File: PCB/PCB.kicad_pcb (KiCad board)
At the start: 2 copper layers, 120 x 60 mm, 62 parts, among them J1 USB_C_Receptacle_USB2.0_16P, J2 Conn_01x15, J3 Conn_01x15, Q2 IRLML2060, SW1 TSA016A2526B, SW2 TSA016A2526B, SW3 TSA016A2526B, U1 RP2040, U2 USBLC6-2SC6, U3 NCP1117ST33T3G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

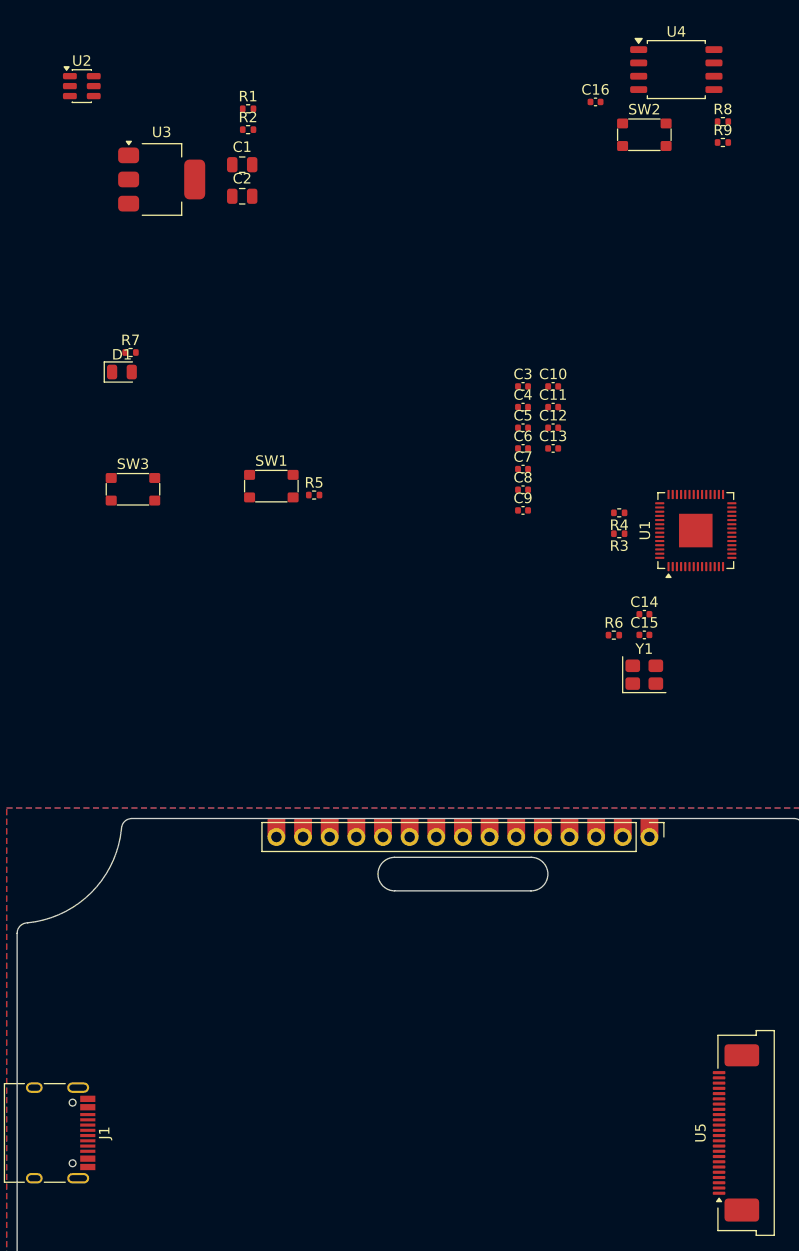
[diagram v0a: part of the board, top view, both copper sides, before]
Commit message: re-wiring a bit for easy routing
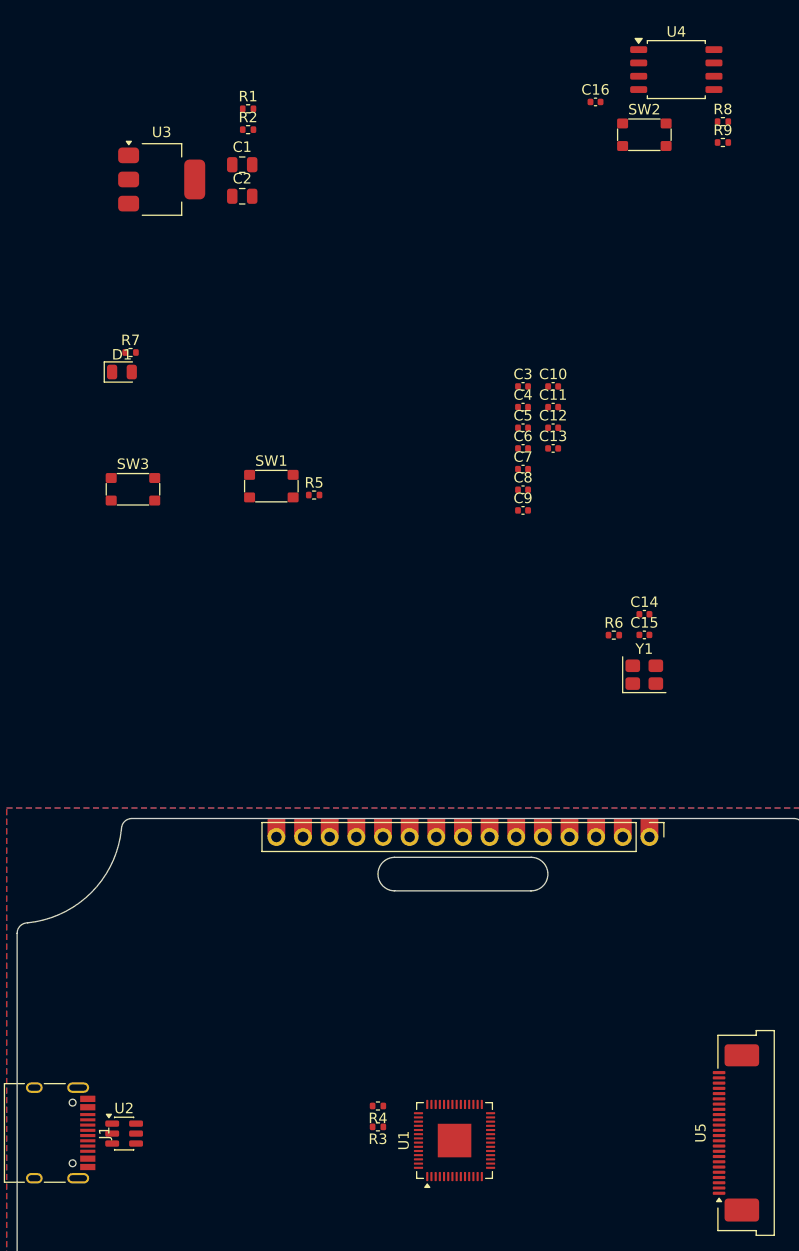
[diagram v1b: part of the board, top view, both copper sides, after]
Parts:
- moved U2 99.9 mm to (80.2, 125.0)
- moved U1 62.5 mm to (111.7, 125.7)
- moved R3 61.0 mm to (104.4, 124.4)
- moved R4 61.0 mm to (104.4, 122.4)
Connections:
- J2 pad 10: /GPIO15 -> /GPIO5
- J2 pad 11: /GPIO16 -> /GPIO6
- J2 pad 12: /GPIO17 -> /GPIO7
- J2 pad 14: /GPIO18 -> /GPIO8
- J2 pad 15: /GPIO19 -> /GPIO9
- J2 pad 2: /GPIO10 -> /GPIO0
- J2 pad 4: /GPIO11 -> /GPIO1
- J2 pad 6: /GPIO12 -> /GPIO2
- J2 pad 7: /GPIO13 -> /GPIO3
- J2 pad 9: /GPIO14 -> /GPIO4
- U1 pad 11: /NFC_GPO -> /GPIO8
- U1 pad 13: /GPIO10 -> /GPIO9
- U1 pad 14: /GPIO11 -> /NFC_SDA
- U1 pad 15: /GPIO12 -> /NFC_SCL
- U1 pad 16: /GPIO13 -> /NFC_GPO
- U1 pad 17: /GPIO14 -> /EPD_DC
- U1 pad 18: /GPIO15 -> /EPD_SCK
- U1 pad 2: /EPD_BUSY -> /GPIO0
- U1 pad 27: /GPIO16 -> /EPD_MOSI
- U1 pad 28: /GPIO17 -> /EPD_BUSY
- U1 pad 29: /GPIO18 -> /EPD_CS
- U1 pad 3: /EPD_CS -> /GPIO1
- U1 pad 30: /GPIO19 -> /EPD_RST
- U1 pad 4: /EPD_SCK -> /GPIO2
- U1 pad 5: /EPD_MOSI -> /GPIO3
- U1 pad 6: /EPD_RST -> /GPIO4
- U1 pad 7: /EPD_DC -> /GPIO5
- U1 pad 8: /NFC_SDA -> /GPIO6
- U1 pad 9: /NFC_SCL -> /GPIO7

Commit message: re-wiring some more stuff, also laying out some stuff
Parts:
- moved C16 150.3 mm to (78.1, 169.4)
- moved R8 150.3 mm to (90.2, 171.3)
- moved R9 150.3 mm to (90.2, 173.3)
- moved SW2 150.3 mm to (82.7, 172.5)
- moved U4 110.2 mm to (104.4, 130.1), turned to 90 degrees
- moved R4 1.97 mm to (106.2, 123.2)
- moved R3 1.81 mm to (106.2, 124.2)
- moved U1 0.91 mm to (111.7, 124.8)
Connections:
- U1 pad 17: /EPD_DC -> /EPD_BUSY
- U1 pad 28: /EPD_BUSY -> /EPD_DC
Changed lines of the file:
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@@
 	(footprint "Capacitor_SMD:C_0402_1005Metric"
 		(layer "F.Cu")
-		(at 125.14 26.69)
+		(at 78.09 169.39)
 		(descr "Capacitor SMD 0402 (1005 Metric), square (rectangular) end terminal, IPC-7351 nominal, (Body size source: IPC-SM-782 page 76, https://www.pcb-3d.com/wordpress/wp-content/uploads/ipc-sm-782a_amendment_1_and_2.pdf), generated with kicad-footprint-generator")
 		(tags "capacitor")
@@
 	(footprint "Package_DFN_QFN:QFN-56-1EP_7x7mm_P0.4mm_EP3.2x3.2mm"
 		(layer "F.Cu")
-		(at 111.7 125.698 90)
+		(at 111.7 124.788998 90)
 		(descr "QFN, 56 Pin (https://datasheets.raspberrypi.com/rp2040/rp2040-datasheet.pdf#page=607), generated with kicad-footprint-generator ipc_noLead_generator.py")
 		(tags "QFN NoLead")
@@
 			(layers "F.Cu" "F.Mask" "F.Paste")
 			(roundrect_rratio 0.25)
-			(net 49 "/EPD_DC")
+			(net 59 "/EPD_BUSY")
 			(pinfunction "GPIO14")
 			(pintype "bidirectional")
@@
 			(layers "F.Cu" "F.Mask" "F.Paste")
 			(roundrect_rratio 0.25)
-			(net 59 "/EPD_BUSY")
+			(net 49 "/EPD_DC")
 			(pinfunction "GPIO17")
 			(pintype "bidirectional")
@@
 	(footprint "Package_SO:SOIC-8_5.3x5.3mm_P1.27mm"
 		(layer "F.Cu")
-		(at 132.8425 23.605)
+		(at 104.4 130.05 90)
 		(descr "SOIC, 8 Pin (JEITA/EIAJ ED-7311-19 variation 08-001-BBA and Atmel/Microchip, 208 mils width, https://www.jeita.or.jp/japanese/standard/book/ED-7311-19/#target/page_no=21, https://ww1.microchip.com/downloads/en/DeviceDoc/20005045C.pdf#page=23, https://ww1.microchip.com/downloads/en/DeviceDoc/doc2535.pdf#page=162), generated with kicad-footprint-generator ipc_gullwing_generator.py")
 		(tags "SOIC SO P-SOP SOP SOP-8 SO SO-8 8S2 S2AE/F K04-056 CASE-751BE SO8W 8-Pin-SOIC PSA W8-2 W8-4 W8MS-1 FPT-8P-M08")
 		(property "Reference" "U4"
-			(at 0 -3.6 0)
+			(at 0 -3.6 90)
 			(layer "F.SilkS")
 			(effects
@@
 		)
 		(property "Value" "W25Q32JVSS"
-			(at 0 3.6 0)
+			(at 0 3.6 90)
 			(layer "F.Fab")
 			(effects
@@
 		)
 		(property "Datasheet" "http://www.winbond.com/resource-files/w25q32jv%20revg%2003272018%20plus.pdf"
-			(at 0 0 0)
+			(at 0 0 90)
 			(layer "F.Fab")
 			(hide yes)
@@
 		)
 		(property "Description" "32Mbit / 4MiB Serial Flash Memory, Standard/Dual/Quad SPI, 2.7-3.6V, SOIC-8 (208 mil)"
-			(at 0 0 0)
+			(at 0 0 90)
 			(layer "F.Fab")
 			(hide yes)
@@
 		(attr smd)
 		(fp_line
-			(start -2.76 -2.76)
-			(end 2.76 -2.76)
+			(start 2.76 -2.76)
+			(end 2.76 -2.49)
 			(stroke
 				(width 0.12)
@@
 		)
 		(fp_line
-			(start -2.76 -2.49)
-			(end -2.76 -2.76)
+			(start -2.76 -2.76)
+			(end 2.76 -2.76)
 			(stroke
 				(width 0.12)
@@
 		)
 		(fp_line
-			(start -2.76 2.76)
-			(end -2.76 2.49)
+			(start -2.76 -2.49)
+			(end -2.76 -2.76)
 			(stroke
 				(width 0.12)
@@
 		)
 		(fp_line
-			(start 2.76 -2.76)
-			(end 2.76 -2.49)
+			(start 2.76 2.49)
+			(end 2.76 2.76)
 			(stroke
 				(width 0.12)
@@
 		)
 		(fp_line
-			(start 2.76 2.49)
-			(end 2.76 2.76)
+			(start 2.76 2.76)
+			(end -2.76 2.76)
 			(stroke
 				(width 0.12)
@@
 		)
 		(fp_line
-			(start 2.76 2.76)
-			(end -2.76 2.76)
+			(start -2.76 2.76)
+			(end -2.76 2.49)
 			(stroke
 				(width 0.12)
@@
 		)
 		(fp_line
-			(start -4.65 -2.48)
-			(end -2.9 -2.48)
+			(start 2.9 -2.9)
+			(end 2.9 -2.48)
 			(stroke
 				(width 0.05)
@@
 		)
 		(fp_line
-			(start -4.65 2.48)
-			(end -4.65 -2.48)
+			(start -2.9 -2.9)
+			(end 2.9 -2.9)
 			(stroke
 				(width 0.05)
@@
 		)
 		(fp_line
-			(start -2.9 -2.9)
-			(end 2.9 -2.9)
+			(start 4.65 -2.48)
+			(end 4.65 2.48)
 			(stroke
 				(width 0.05)
@@
 		)
 		(fp_line
-			(start -2.9 -2.48)
-			(end -2.9 -2.9)
+			(start 2.9 -2.48)
+			(end 4.65 -2.48)
 			(stroke
 				(width 0.05)
@@
 		)
 		(fp_line
-			(start -2.9 2.48)
-			(end -4.65 2.48)
+			(start -2.9 -2.48)
+			(end -2.9 -2.9)
 			(stroke
 				(width 0.05)
@@
 		)
 		(fp_line
-			(start -2.9 2.9)
-			(end -2.9 2.48)
+			(start -4.65 -2.48)
+			(end -2.9 -2.48)
 			(stroke
 				(width 0.05)
@@
 		)
 		(fp_line
-			(start 2.9 -2.9)
-			(end 2.9 -2.48)
+			(start 4.65 2.48)
+			(end 2.9 2.48)
 			(stroke
 				(width 0.05)
@@
 		)
 		(fp_line
-			(start 2.9 -2.48)
-			(end 4.65 -2.48)
+			(start 2.9 2.48)
+			(end 2.9 2.9)
 			(stroke
 				(width 0.05)
@@
 		)
 		(fp_line
-			(start 2.9 2.48)
-			(end 2.9 2.9)
+			(start -2.9 2.48)
+			(end -4.65 2.48)
 			(stroke
 				(width 0.05)
@@
 		)
 		(fp_line
-			(start 2.9 2.9)
-			(end -2.9 2.9)
+			(start -4.65 2.48)
+			(end -4.65 -2.48)
 			(stroke
 				(width 0.05)
@@
 		)
 		(fp_line
-			(start 4.65 -2.48)
-			(end 4.65 2.48)
+			(start 2.9 2.9)
+			(end -2.9 2.9)
 			(stroke
 				(width 0.05)
@@
 		)
 		(fp_line
-			(start 4.65 2.48)
-			(end 2.9 2.48)
+			(start -2.9 2.9)
+			(end -2.9 2.48)
 			(stroke
 				(width 0.05)
@@
 		)
 		(fp_text user "${REFERENCE}"
-			(at 0 0 0)
+			(at 0 0 90)
 			(layer "F.Fab")
 			(effects
@@
 		)
 		(pad "1" smd roundrect
-			(at -3.5875 -1.905)
+			(at -3.5875 -1.905 90)
 			(size 1.625 0.65)
 			(layers "F.Cu" "F.Mask" "F.Paste")
@@
 		)
 		(pad "2" smd roundrect
-			(at -3.5875 -0.635)
+			(at -3.5875 -0.635 90)
 			(size 1.625 0.65)
 			(layers "F.Cu" "F.Mask" "F.Paste")
@@
 		)
 		(pad "3" smd roundrect
-			(at -3.5875 0.635)
+			(at -3.5875 0.635 90)
 			(size 1.625 0.65)
 			(layers "F.Cu" "F.Mask" "F.Paste")
@@
 		)
 		(pad "4" smd roundrect
-			(at -3.5875 1.905)
+			(at -3.5875 1.905 90)
 			(size 1.625 0.65)
 			(layers "F.Cu" "F.Mask" "F.Paste")
@@
 		)
 		(pad "5" smd roundrect
-			(at 3.5875 1.905)
+			(at 3.5875 1.905 90)
 			(size 1.625 0.65)
 			(layers "F.Cu" "F.Mask" "F.Paste")
@@
 		)
 		(pad "6" smd roundrect
-			(at 3.5875 0.635)
+			(at 3.5875 0.635 90)
 			(size 1.625 0.65)
 			(layers "F.Cu" "F.Mask" "F.Paste")
@@
 		)
 		(pad "7" smd roundrect
-			(at 3.5875 -0.635)
+			(at 3.5875 -0.635 90)
 			(size 1.625 0.65)
 			(layers "F.Cu" "F.Mask" "F.Paste")
@@
 		)
 		(pad "8" smd roundrect
-			(at 3.5875 -1.905)
+			(at 3.5875 -1.905 90)
 			(size 1.625 0.65)
 			(layers "F.Cu" "F.Mask" "F.Paste")
@@
 	(footprint "Resistor_SMD:R_0402_1005Metric"
 		(layer "F.Cu")
-		(at 104.4 124.398 180)
+		(at 106.2 124.25 180)
 		(descr "Resistor SMD 0402 (1005 Metric), square (rectangular) end terminal, IPC-7351 nominal, (Body size source: IPC-SM-782 page 72, https://www.pcb-3d.com/wordpress/wp-content/uploads/ipc-sm-782a_amendment_1_and_2.pdf), generated with kicad-footprint-generator")
 		(tags "resistor")
@@
 	(footprint "Resistor_SMD:R_0402_1005Metric"
 		(layer "F.Cu")
-		(at 137.285 30.555)
+		(at 90.235 173.255)
 		(descr "Resistor SMD 0402 (1005 Metric), square (rectangular) end terminal, IPC-7351 nominal, (Body size source: IPC-SM-782 page 72, https://www.pcb-3d.com/wordpress/wp-content/uploads/ipc-sm-782a_amendment_1_and_2.pdf), generated with kicad-footprint-generator")
 		(tags "resistor")
@@
 	(footprint "Resistor_SMD:R_0402_1005Metric"
 		(layer "F.Cu")
-		(at 137.285 28.565)
+		(at 90.235 171.265)
 		(descr "Resistor SMD 0402 (1005 Metric), square (rectangular) end terminal, IPC-7351 nominal, (Body size source: IPC-SM-782 page 72, https://www.pcb-3d.com/wordpress/wp-content/uploads/ipc-sm-782a_amendment_1_and_2.pdf), generated with kicad-footprint-generator")
 		(tags "resistor")
@@
 	(footprint "kai's library:SW_Push_SPST_TSA016"
 		(layer "F.Cu")
-		(at 129.795 29.815)
+		(at 82.745 172.515)
 		(property "Reference" "SW2"
 			(at 0 -2.4 0)
@@
 	(footprint "Resistor_SMD:R_0402_1005Metric"
 		(layer "F.Cu")
-		(at 104.4 122.408 180)
+		(at 106.2 123.2 180)
 		(descr "Resistor SMD 0402 (1005 Metric), square (rectangular) end terminal, IPC-7351 nominal, (Body size source: IPC-SM-782 page 72, https://www.pcb-3d.com/wordpress/wp-content/uploads/ipc-sm-782a_amendment_1_and_2.pdf), generated with kicad-footprint-generator")
 		(tags "resistor")

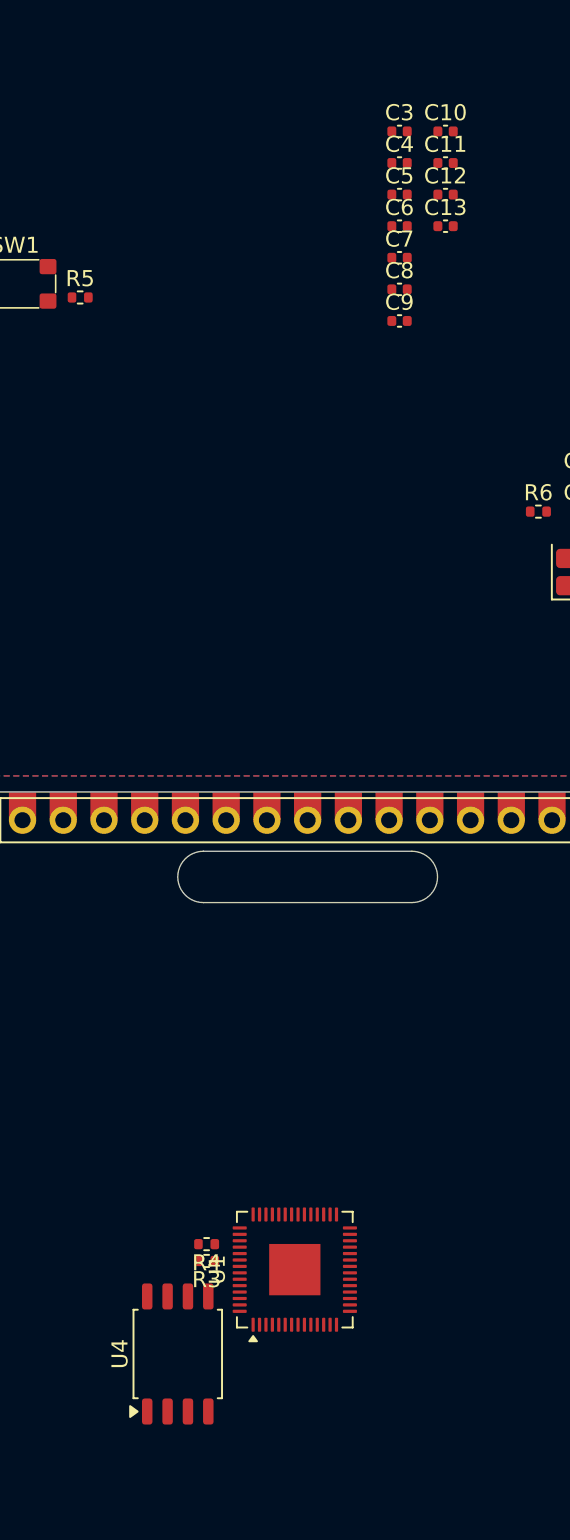
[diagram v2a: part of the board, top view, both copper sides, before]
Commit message: aligning the caps
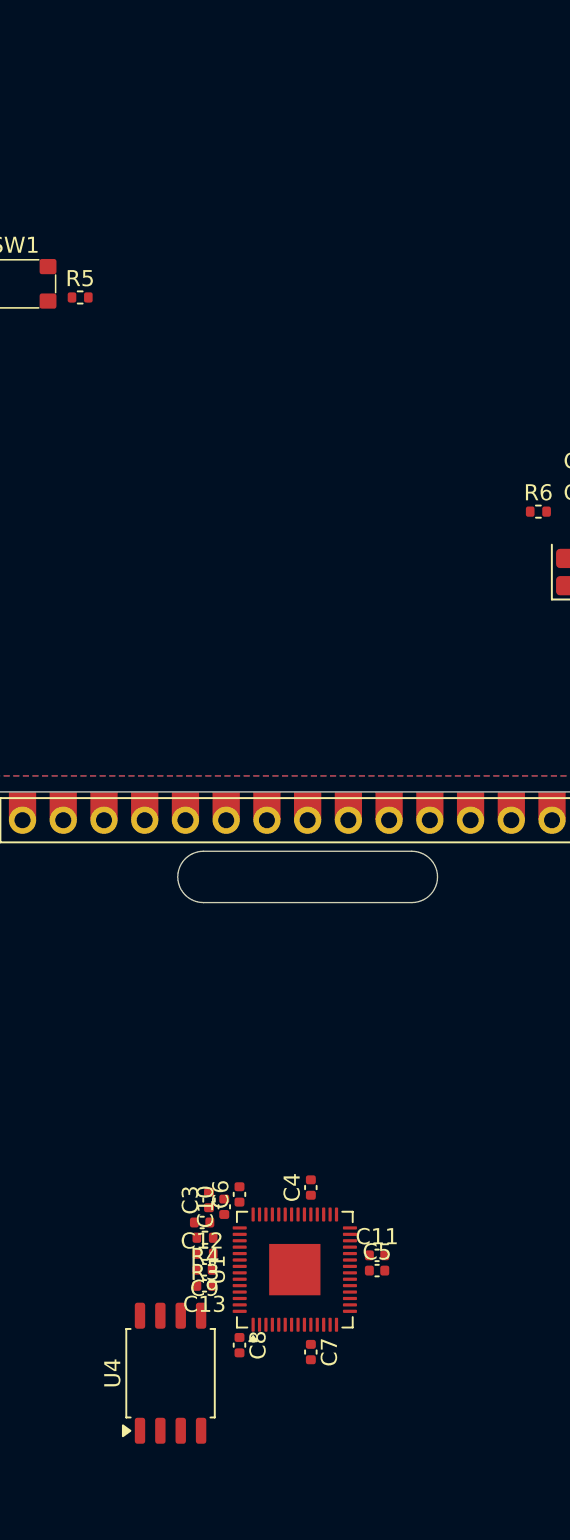
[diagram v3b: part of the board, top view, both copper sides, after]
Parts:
- moved C10 68.5 mm to (107.3, 120.9), turned to 90 degrees
- moved C7 68.5 mm to (112.7, 129.9), turned to -90 degrees
- moved C11 68.3 mm to (116.8, 123.9)
- moved C13 67.8 mm to (106.1, 125.8), turned to 180 degrees
- moved C3 67.7 mm to (106.3, 120.5), turned to 90 degrees
- moved C5 67.1 mm to (116.8, 124.8)
- moved C8 66.6 mm to (108.2, 129.5), turned to -90 degrees
- moved C12 65.9 mm to (105.9, 121.8), turned to 180 degrees
- moved C4 64.1 mm to (112.7, 119.7), turned to 90 degrees
- moved C6 61.2 mm to (108.2, 120.1), turned to 90 degrees
- moved C9 60.4 mm to (106.1, 124.8), turned to 180 degrees
- moved U4 1.28 mm to (104.0, 131.2)
- moved R3 0.46 mm to (106.1, 123.8)
- moved R4 0.41 mm to (106.1, 122.8)
